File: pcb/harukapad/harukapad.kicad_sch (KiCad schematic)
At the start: 65 parts, among them J1 USB_C_Receptacle_USB2.0, SW1 SW_Push, SW2 SW_Push, U1 SRV05-4, U2 XC6206P332MR, U3 DRV5056A4xDBZxQ1, U4 DRV5056A4xDBZxQ1, U5 DRV5056A4xDBZxQ1, U6 74AHCT1G125, U7 74AHCT1G125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

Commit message: feat: add minoripad
this is a simplified version of the harukapad, with regular MX switches and no RGB effects.

will be used to validate my case design.
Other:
- title: Haruka (Analog PCB ver.) -> Harukapad

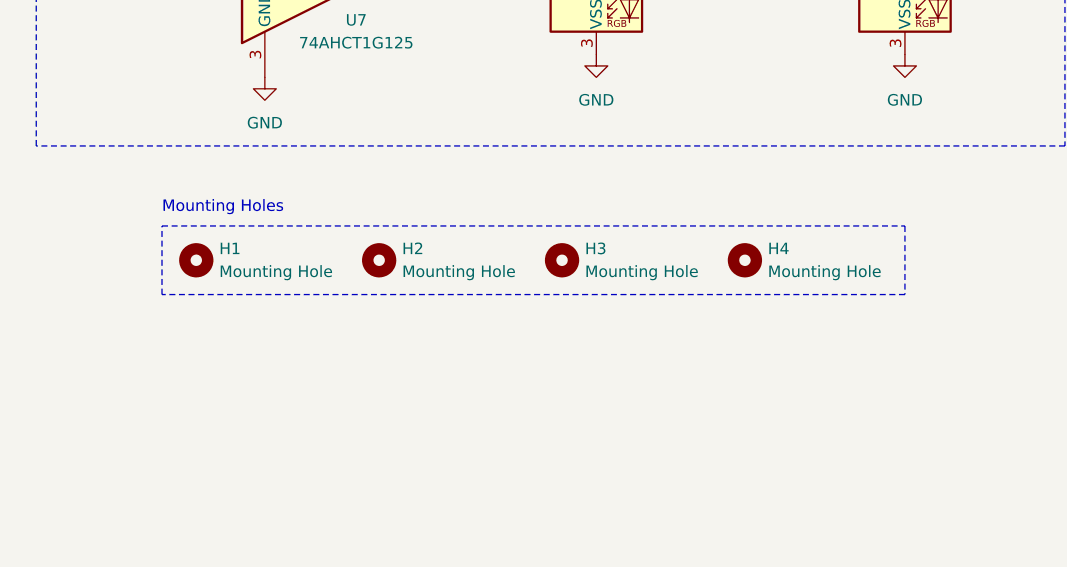
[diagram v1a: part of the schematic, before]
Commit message: fix(harukapad): connect mounting holes to ground, fix incorrect footprint
at some point, it changed back to the SOT-23 footprint, so the holes would've been missing...
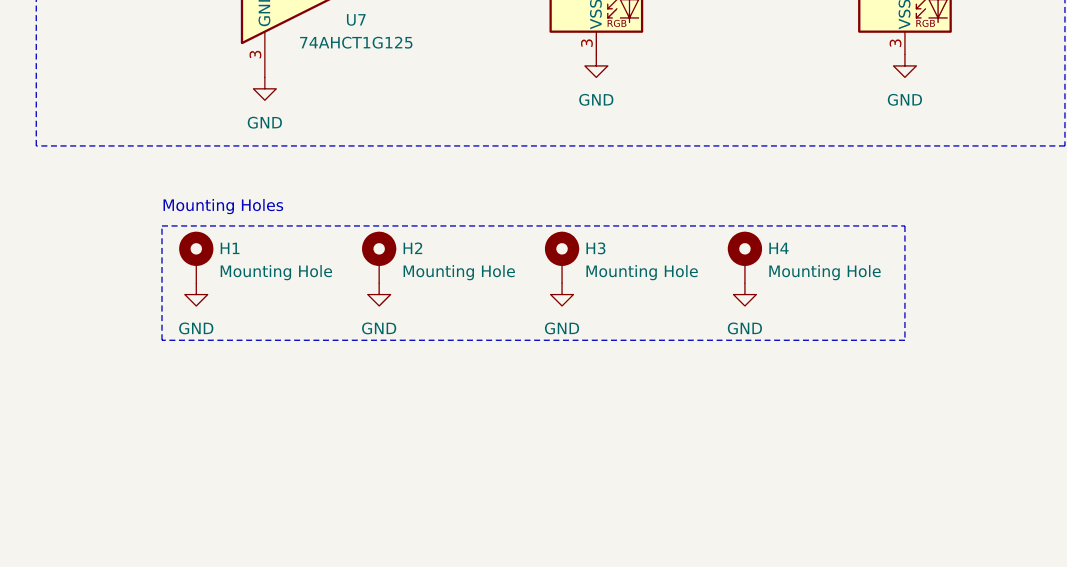
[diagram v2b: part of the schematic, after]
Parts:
- H1, H2, H3, H4: symbol Mechanical:MountingHole -> Mechanical:MountingHole_Pad
- U3, U4, U5: footprint Package_TO_SOT_SMD:SOT-23 -> Custom:KS-20-1U-DRV5056
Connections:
- net GND: now also H1.1, H2.1, H3.1, H4.1
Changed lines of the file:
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@@
     (fill (type none))
   )
-  (rectangle (start 173.99 168.91) (end 256.54 176.53)
+  (rectangle (start 173.99 168.91) (end 256.54 181.61)
     (stroke (width 0) (type dash))
     (fill (type none))
@@
     )
   )
+  (symbol (lib_id "power:GND") (at 198.12 175.26 0) (unit 1)
+    (in_bom yes) (on_board yes) (dnp no) (fields_autoplaced)
+    (property "Reference" "#PWR059" (at 198.12 181.61 0)
+      (effects (font (size 1.27 1.27)) hide)
+    )
+    (property "Value" "GND" (at 198.12 180.34 0)
+      (effects (font (size 1.27 1.27)))
+    )
+    (property "Footprint" "" (at 198.12 175.26 0)
+      (effects (font (size 1.27 1.27)) hide)
+    )
+    (property "Datasheet" "" (at 198.12 175.26 0)
+      (effects (font (size 1.27 1.27)) hide)
+    )
+    (pin "1")
+    (instances
+      (project "harukapad"
+        (path "/a63f8075-a969-4b1c-b924-6f5af0e1e9e2"
+          (reference "#PWR059") (unit 1)
+        )
+      )
+      (project "harukapad"
+        (path "/fe0c1c23-b294-4653-a8db-85682224ef67"
+          (reference "#PWR060") (unit 1)
+        )
+      )
+    )
+  )
   (symbol (lib_id "power:GND") (at 266.7 99.06 0) (unit 1)
     (in_bom yes) (on_board yes) (dnp no) (fields_autoplaced)
@@
     )
   )
+  (symbol (lib_id "power:GND") (at 218.44 175.26 0) (unit 1)
+    (in_bom yes) (on_board yes) (dnp no) (fields_autoplaced)
+    (property "Reference" "#PWR060" (at 218.44 181.61 0)
+      (effects (font (size 1.27 1.27)) hide)
+    )
+    (property "Value" "GND" (at 218.44 180.34 0)
+      (effects (font (size 1.27 1.27)))
+    )
+    (property "Footprint" "" (at 218.44 175.26 0)
+      (effects (font (size 1.27 1.27)) hide)
+    )
+    (property "Datasheet" "" (at 218.44 175.26 0)
+      (effects (font (size 1.27 1.27)) hide)
+    )
+    (pin "1")
+    (instances
+      (project "harukapad"
+        (path "/a63f8075-a969-4b1c-b924-6f5af0e1e9e2"
+          (reference "#PWR060") (unit 1)
+        )
+      )
+      (project "harukapad"
+        (path "/fe0c1c23-b294-4653-a8db-85682224ef67"
+          (reference "#PWR060") (unit 1)
+        )
+      )
+    )
+  )
   (symbol (lib_id "Device:C_Small") (at 218.44 81.28 90) (mirror x) (unit 1)
     (in_bom yes) (on_board yes) (dnp no)
@@
       (effects (font (size 1.27 1.27)) (justify right))
     )
-    (property "Footprint" "Package_TO_SOT_SMD:SOT-23" (at 186.69 44.45 0)
+    (property "Footprint" "Custom:KS-20-1U-DRV5056" (at 186.69 44.45 0)
       (effects (font (size 1.27 1.27)) hide)
     )
@@
     )
   )
-  (symbol (lib_id "Mechanical:MountingHole") (at 198.12 172.72 0) (unit 1)
-    (in_bom no) (on_board yes) (dnp no) (fields_autoplaced)
+  (symbol (lib_id "Mechanical:MountingHole_Pad") (at 198.12 172.72 0) (unit 1)
+    (in_bom no) (on_board yes) (dnp no)
     (property "Reference" "H2" (at 200.66 171.45 0)
       (effects (font (size 1.27 1.27)) (justify left))
@@
       (effects (font (size 1.27 1.27)) hide)
     )
+    (pin "1")
     (instances
       (project "harukapad"
@@
       (effects (font (size 1.27 1.27)) (justify right))
     )
-    (property "Footprint" "Package_TO_SOT_SMD:SOT-23" (at 303.53 44.45 0)
+    (property "Footprint" "Custom:KS-20-1U-DRV5056" (at 303.53 44.45 0)
       (effects (font (size 1.27 1.27)) hide)
     )
@@
     )
   )
-  (symbol (lib_id "Mechanical:MountingHole") (at 218.44 172.72 0) (unit 1)
-    (in_bom no) (on_board yes) (dnp no) (fields_autoplaced)
+  (symbol (lib_id "Mechanical:MountingHole_Pad") (at 218.44 172.72 0) (unit 1)
+    (in_bom no) (on_board yes) (dnp no)
     (property "Reference" "H3" (at 220.98 171.45 0)
       (effects (font (size 1.27 1.27)) (justify left))
@@
       (effects (font (size 1.27 1.27)) hide)
     )
+    (pin "1")
     (instances
       (project "harukapad"
@@
       (effects (font (size 1.27 1.27)) (justify right))
     )
-    (property "Footprint" "Package_TO_SOT_SMD:SOT-23" (at 245.11 44.45 0)
+    (property "Footprint" "Custom:KS-20-1U-DRV5056" (at 245.11 44.45 0)
       (effects (font (size 1.27 1.27)) hide)
     )
@@
     )
   )
+  (symbol (lib_id "power:GND") (at 177.8 175.26 0) (unit 1)
+    (in_bom yes) (on_board yes) (dnp no) (fields_autoplaced)
+    (property "Reference" "#PWR058" (at 177.8 181.61 0)
+      (effects (font (size 1.27 1.27)) hide)
+    )
+    (property "Value" "GND" (at 177.8 180.34 0)
+      (effects (font (size 1.27 1.27)))
+    )
+    (property "Footprint" "" (at 177.8 175.26 0)
+      (effects (font (size 1.27 1.27)) hide)
+    )
+    (property "Datasheet" "" (at 177.8 175.26 0)
+      (effects (font (size 1.27 1.27)) hide)
+    )
+    (pin "1")
+    (instances
+      (project "harukapad"
+        (path "/a63f8075-a969-4b1c-b924-6f5af0e1e9e2"
+          (reference "#PWR058") (unit 1)
+        )
+      )
+      (project "harukapad"
+        (path "/fe0c1c23-b294-4653-a8db-85682224ef67"
+          (reference "#PWR060") (unit 1)
+        )
+      )
+    )
+  )
   (symbol (lib_id "Device:R_Small") (at 199.39 81.28 90) (unit 1)
     (in_bom yes) (on_board yes) (dnp no)
@@
     )
   )
+  (symbol (lib_id "power:GND") (at 238.76 175.26 0) (unit 1)
+    (in_bom yes) (on_board yes) (dnp no) (fields_autoplaced)
+    (property "Reference" "#PWR061" (at 238.76 181.61 0)
+      (effects (font (size 1.27 1.27)) hide)
+    )
+    (property "Value" "GND" (at 238.76 180.34 0)
+      (effects (font (size 1.27 1.27)))
+    )
+    (property "Footprint" "" (at 238.76 175.26 0)
+      (effects (font (size 1.27 1.27)) hide)
+    )
+    (property "Datasheet" "" (at 238.76 175.26 0)
+      (effects (font (size 1.27 1.27)) hide)
+    )
+    (pin "1")
+    (instances
+      (project "harukapad"
+        (path "/a63f8075-a969-4b1c-b924-6f5af0e1e9e2"
+          (reference "#PWR061") (unit 1)
+        )
+      )
+      (project "harukapad"
+        (path "/fe0c1c23-b294-4653-a8db-85682224ef67"
+          (reference "#PWR060") (unit 1)
+        )
+      )
+    )
+  )
   (symbol (lib_id "power:GND") (at 184.15 54.61 0) (unit 1)
     (in_bom yes) (on_board yes) (dnp no) (fields_autoplaced)
@@
     )
   )
-  (symbol (lib_id "Mechanical:MountingHole") (at 177.8 172.72 0) (unit 1)
+  (symbol (lib_id "Mechanical:MountingHole_Pad") (at 177.8 172.72 0) (unit 1)
     (in_bom no) (on_board yes) (dnp no)
     (property "Reference" "H1" (at 180.34 171.45 0)
@@
       (effects (font (size 1.27 1.27)) hide)
     )
+    (pin "1")
     (instances
       (project "harukapad"
@@
     )
   )
-  (symbol (lib_id "Mechanical:MountingHole") (at 238.76 172.72 0) (unit 1)
-    (in_bom no) (on_board yes) (dnp no) (fields_autoplaced)
+  (symbol (lib_id "Mechanical:MountingHole_Pad") (at 238.76 172.72 0) (unit 1)
+    (in_bom no) (on_board yes) (dnp no)
     (property "Reference" "H4" (at 241.3 171.45 0)
       (effects (font (size 1.27 1.27)) (justify left))
@@
       (effects (font (size 1.27 1.27)) hide)
     )
+    (pin "1")
     (instances
       (project "harukapad"
